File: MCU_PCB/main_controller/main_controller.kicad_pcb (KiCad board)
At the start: 2 copper layers, 127 x 101.7 mm, 62 parts, among them IC5 esp-12f, J1 TB006-508-05BE, J2 TB006-508-05BE, J4 TB006-508-05BE, J5 1715250000, J8 USB_B_Micro, Q2 S8050, Q3 S8050, SW1 SW_SPDT, U1 STM32F446ZET6, U3 CH340G, U4 R-78E5.0-0.5, U5 ISE0512A-H, X1 ECS-2520MV-xxx-xx, Y1 Crystal_GND24_Small

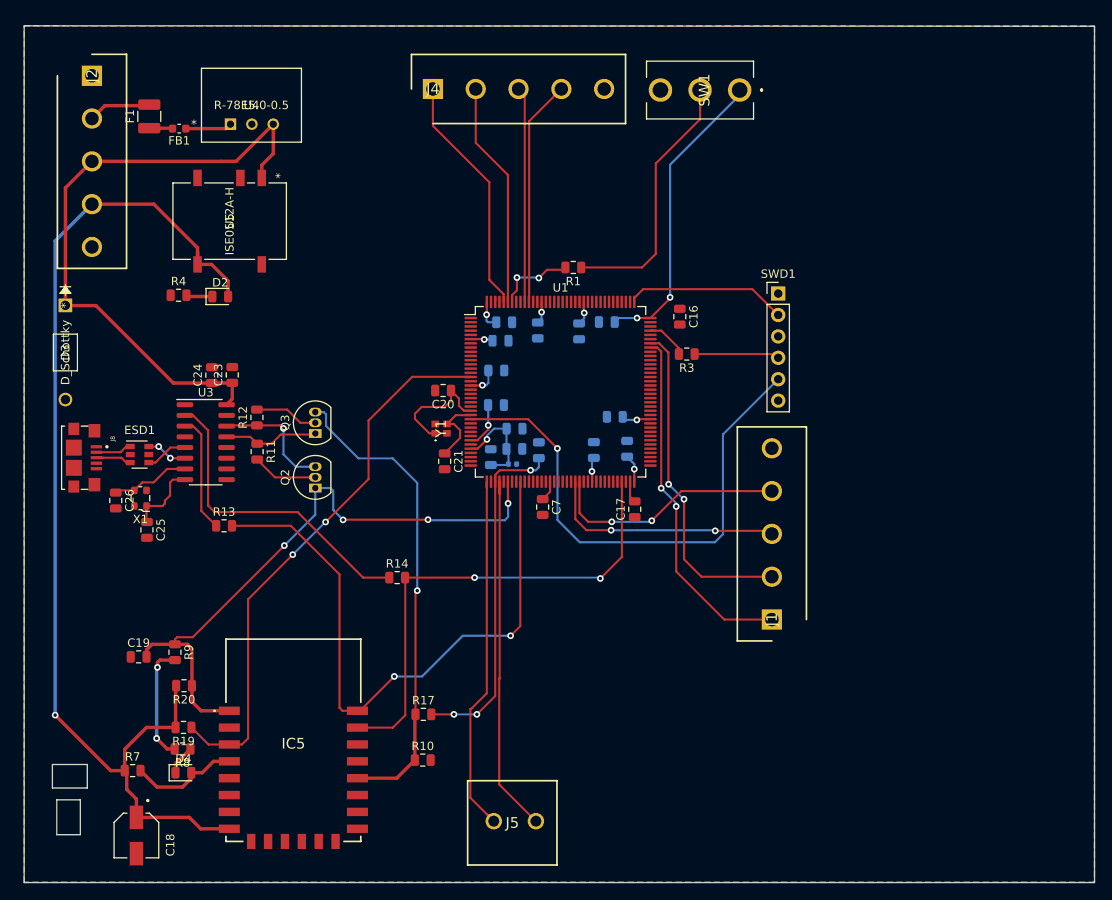
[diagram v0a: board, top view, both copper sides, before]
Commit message: finished drc check
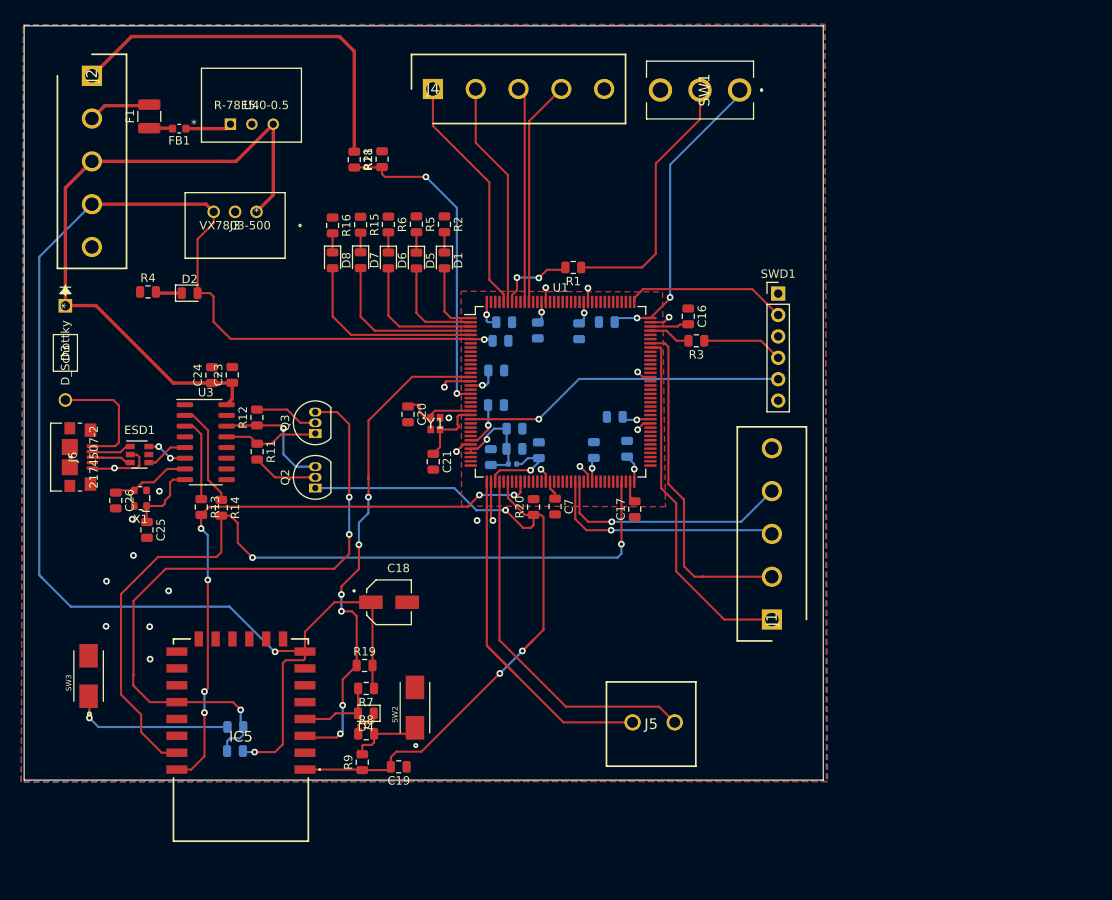
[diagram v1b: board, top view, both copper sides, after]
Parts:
- removed J8: USB_B_Micro, usbtomicro:J_SMD_2174507-2-5_7.8_5_2.71
- removed U5: ISE0512A-H, 5to3.3:ISE0512A-H
- added D1: LED, LED_SMD:LED_0805_2012Metric, F.Cu at (151.8, 54.7)
- added D5: LED, LED_SMD:LED_0805_2012Metric, F.Cu at (148.5, 54.7)
- added D6: LED, LED_SMD:LED_0805_2012Metric, F.Cu at (145.2, 54.7)
- added D7: LED, LED_SMD:LED_0805_2012Metric, F.Cu at (141.9, 54.7)
- added D8: LED, LED_SMD:LED_0805_2012Metric, F.Cu at (138.6, 54.7)
- added J3: VX7803-500, NEW5TO3V3:VX7803-500, F.Cu at (129.6, 49.0)
- added J6: 2174507-2, microusb_b:2174507-2, F.Cu at (107.7, 78.1)
- added R15: R, Resistor_SMD:R_0805_2012Metric, F.Cu at (141.9, 50.5)
- added R16: R, Resistor_SMD:R_0805_2012Metric, F.Cu at (138.6, 50.6)
- added R18: 10k, Resistor_SMD:R_0805_2012Metric, F.Cu at (141.2, 42.8)
- added R2: R, Resistor_SMD:R_0805_2012Metric, F.Cu at (151.8, 50.4)
- added R21: 2k, Resistor_SMD:R_0805_2012Metric, F.Cu at (144.4, 42.7)
- added R5: R, Resistor_SMD:R_0805_2012Metric, F.Cu at (148.5, 50.4)
- added R6: R, Resistor_SMD:R_0805_2012Metric, F.Cu at (145.2, 50.5)
- added SW2: KEY_USER, pushbutton:SW_147873-2, F.Cu at (148.3, 107.8)
- added SW3: KEY_FLASH, pushbutton:SW_147873-2, F.Cu at (109.6, 104.0)
- R10, R17: moved to B.Cu
- moved R20 46.6 mm to (162.4, 84.0), turned to 90 degrees
- moved C18 40.8 mm to (145.3, 95.3), turned to 0 degrees
- moved C19 33.5 mm to (146.4, 114.8), turned to 180 degrees
- moved R7 29.4 mm to (142.6, 105.5), turned to 180 degrees
- moved R9 25.8 mm to (142.1, 114.2), turned to 90 degrees
- moved R17 22.8 mm to (127.0, 112.9)
- moved D4 22.8 mm to (142.5, 108.5), turned to 180 degrees
- moved R19 22.7 mm to (142.4, 102.8), turned to 0 degrees
- moved R10 22.6 mm to (127.0, 110.1), turned to 180 degrees
- moved R14 22.4 mm to (125.4, 84.1), turned to 270 degrees
- moved R8 21.9 mm to (142.6, 110.9), turned to 0 degrees
- moved J5 20.2 mm to (179.2, 109.5)
- moved IC5 6.23 mm to (127.7, 111.6), turned to 180 degrees
- moved C20 5.03 mm to (147.5, 73.0), turned to 270 degrees
- moved D2 3.65 mm to (121.6, 58.6)
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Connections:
- U1 pad 1: Net-(U1-Pad1) -> GPIO_LED1
- U1 pad 2: Net-(U1-Pad2) -> GPIO_LED2
- U1 pad 3: Net-(U1-Pad3) -> GPIO_LED3
- U1 pad 35: TIM2_CH2 -> Net-(U1-Pad35)
- U1 pad 4: Net-(U1-Pad4) -> GPIO_LED4
- U1 pad 5: Net-(U1-Pad5) -> GPIO_LED5
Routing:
- net 12V: track 0.00 -> 45.7 mm
- net USART1_TX: track 58.4 -> 100.6 mm
- net ADC3_IN5: track 0.00 -> 38.4 mm, vias 0 -> 2
- net GND: track 0.00 -> 32.0 mm, vias 0 -> 21
- net Net-(R14-Pad1): track 37.9 -> 12.8 mm
- net 3V3: track 240.6 -> 264.8 mm, vias 15 -> 14
- net NRST: track 62.5 -> 38.5 mm
- net GPIO_LED5: track 0.00 -> 23.0 mm
- net /WiFi + MCU/GPIO0: track 57.3 -> 78.6 mm, vias 1 -> 3
- net Net-(R10-Pad2): track 0.00 -> 20.1 mm, vias 0 -> 1
- net GPIO_LED4: track 0.00 -> 19.5 mm
- net GPIO_LED3: track 0.00 -> 15.9 mm
- net Net-(D3-Pad2): track 0.00 -> 15.3 mm
- net WIFI_nRST: track 75.0 -> 87.5 mm, vias 4 -> 3
- net GPIO_LED2: track 0.00 -> 12.2 mm
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- added copper zone on F.Cu, net 3V3
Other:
- board size 127 x 101.7 mm -> 94.8 x 89.5 mm

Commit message: Adding footprints/schematics locally
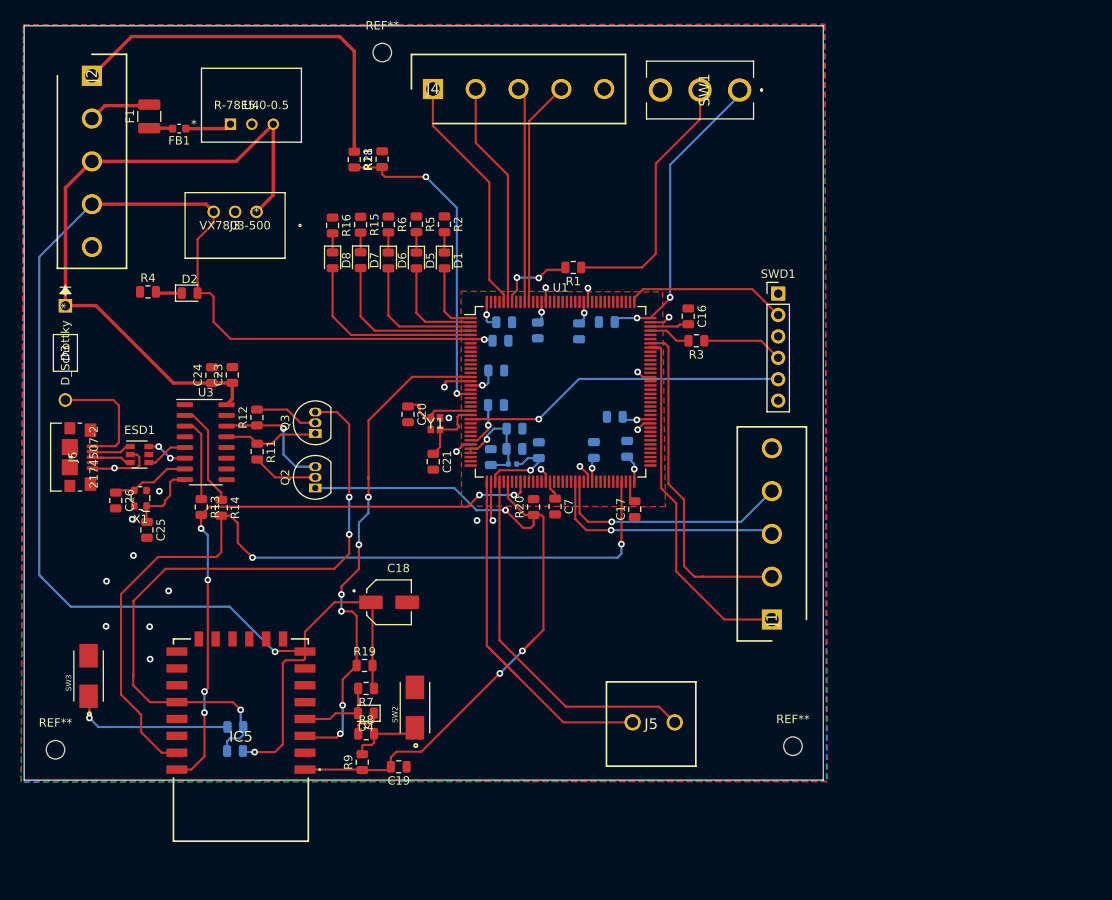
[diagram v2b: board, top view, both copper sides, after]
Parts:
- added REF**: MountingHole_2.2mm_M2, MountingHole:MountingHole_2.2mm_M2, F.Cu at (144.5, 30.1)
- added REF**: MountingHole_2.2mm_M2, MountingHole:MountingHole_2.2mm_M2, F.Cu at (105.7, 112.8)
- added REF**: MountingHole_2.2mm_M2, MountingHole:MountingHole_2.2mm_M2, F.Cu at (193.2, 112.3)
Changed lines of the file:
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@@
   (general
     (thickness 1.6)
-    (drawings 4)
+    (drawings 8)
     (tracks 606)
     (zones 0)
-    (modules 76)
+    (modules 79)
     (nets 185)
   )
@@
     (add_net WIFI_nRST)
   )
+  (module MountingHole:MountingHole_2.2mm_M2 (layer F.Cu)
+    (at 144.475 30.05)
+    (descr "Mounting Hole 2.2mm, no annular, M2")
+    (tags "mounting hole 2.2mm no annular m2")
+    (attr virtual)
+    (fp_text reference REF** (at 0 -3.2) (layer F.SilkS)
+      (effects (font (size 1 1) (thickness 0.15)))
+    )
+    (fp_text value MountingHole_2.2mm_M2 (at 0 3.2) (layer F.Fab)
+      (effects (font (size 1 1) (thickness 0.15)))
+    )
+    (fp_circle (center 0 0) (end 2.2 0) (layer Cmts.User) (width 0.15))
+    (fp_circle (center 0 0) (end 2.45 0) (layer F.CrtYd) (width 0.05))
+    (fp_text user %R (at 0.3 0) (layer F.Fab)
+      (effects (font (size 1 1) (thickness 0.15)))
+    )
+    (pad 1 np_thru_hole circle (at 0 0) (size 2.2 2.2) (drill 2.2) (layers *.Cu *.Mask))
+  )
+  (module MountingHole:MountingHole_2.2mm_M2 (layer F.Cu)
+    (at 105.7 112.775)
+    (descr "Mounting Hole 2.2mm, no annular, M2")
+    (tags "mounting hole 2.2mm no annular m2")
+    (attr virtual)
+    (fp_text reference REF** (at 0 -3.2) (layer F.SilkS)
+      (effects (font (size 1 1) (thickness 0.15)))
+    )
+    (fp_text value MountingHole_2.2mm_M2 (at 0 3.2) (layer F.Fab)
+      (effects (font (size 1 1) (thickness 0.15)))
+    )
+    (fp_circle (center 0 0) (end 2.2 0) (layer Cmts.User) (width 0.15))
+    (fp_circle (center 0 0) (end 2.45 0) (layer F.CrtYd) (width 0.05))
+    (fp_text user %R (at 0.3 0) (layer F.Fab)
+      (effects (font (size 1 1) (thickness 0.15)))
+    )
+    (pad 1 np_thru_hole circle (at 0 0) (size 2.2 2.2) (drill 2.2) (layers *.Cu *.Mask))
+  )
+  (module MountingHole:MountingHole_2.2mm_M2 (layer F.Cu)
+    (at 193.2 112.35)
+    (descr "Mounting Hole 2.2mm, no annular, M2")
+    (tags "mounting hole 2.2mm no annular m2")
+    (attr virtual)
+    (fp_text reference REF** (at 0 -3.2) (layer F.SilkS)
+      (effects (font (size 1 1) (thickness 0.15)))
+    )
+    (fp_text value MountingHole_2.2mm_M2 (at 0 3.2) (layer F.Fab)
+      (effects (font (size 1 1) (thickness 0.15)))
+    )
+    (fp_circle (center 0 0) (end 2.2 0) (layer Cmts.User) (width 0.15))
+    (fp_circle (center 0 0) (end 2.45 0) (layer F.CrtYd) (width 0.05))
+    (fp_text user %R (at 0.3 0) (layer F.Fab)
+      (effects (font (size 1 1) (thickness 0.15)))
+    )
+    (pad 1 np_thru_hole circle (at 0 0) (size 2.2 2.2) (drill 2.2) (layers *.Cu *.Mask))
+  )
   (module NEW5TO3V3:VX7803-500 (layer F.Cu)
     (at 129.55 48.95 180)
@@
       (net 184 "Net-(J6-Pad11)"))
   )
+  (gr_circle (center 138.45 115.075) (end 138.5 115.6) (layer Dwgs.User) (width 0.15))
+  (gr_circle (center 113.05 76.8) (end 113.1 77.325) (layer Dwgs.User) (width 0.15))
+  (gr_circle (center 118.9 71.85) (end 118.95 72.375) (layer Dwgs.User) (width 0.15))
+  (gr_circle (center 153.125 61.45) (end 153.175 61.975) (layer Dwgs.User) (width 0.15))
   (gr_line (start 196.8 26.88) (end 101.983 26.88) (layer Edge.Cuts) (width 0.05))
   (gr_line (start 196.8 116.375) (end 196.8 26.88) (layer Edge.Cuts) (width 0.05))

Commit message: Archived main board
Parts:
- removed the REF** at (144.5, 30.1)
- removed the REF** at (105.7, 112.8)
- removed the REF** at (193.2, 112.3)
- added R22: 0, Resistor_SMD:R_0805_2012Metric, B.Cu at (161.4, 71.4)
- added REF**: MountingHole_2.2mm_M2, MountingHole:MountingHole_2.2mm_M2, F.Cu at (143.0, 32.7)
- added REF**: MountingHole_2.2mm_M2, MountingHole:MountingHole_2.2mm_M2, F.Cu at (192.0, 111.8)
- added REF**: MountingHole_2.2mm_M2, MountingHole:MountingHole_2.2mm_M2, F.Cu at (105.9, 113.2)
- D3: footprint Diode 4007:1N4007G-T -> walle_library:1N4007G-T
- IC5: footprint esp12f -> walle_library:esp12f
- J3: footprint NEW5TO3V3:VX7803-500 -> walle_library:VX7803-500
- J6: footprint microusb_b:2174507-2 -> walle_library:2174507-2
- SW1: footprint spdt switch:118251376 -> walle_library:118251376
- SW2, SW3: footprint pushbutton:SW_147873-2 -> walle_library:SW_147873-2
- U4: footprint DC 7.5 to 5:R-78E5.0-0.5 -> walle_library:R-78E5.0-0.5
- Y1: footprint EA1620LA12-16.000M_TR:EA1620LA1216000MTR -> walle_library:EA1620LA1216000MTR
- moved R18 3.75 mm to (138.6, 45.5)
- moved R21 3.75 mm to (141.9, 45.4)
- moved C15 2.45 mm to (160.2, 74.6), turned to 180 degrees
- moved C14 2.35 mm to (160.2, 77.0), turned to 180 degrees
- moved C5 1.40 mm to (157.4, 76.7)
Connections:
- C14 pad 2: GND -> /AGND
- C15 pad 2: GND -> /AGND
- C5 pad 2: GND -> /AGND
- SWD1 pad 1: 3.3V_regulator -> 3V3
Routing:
- net 3V3: track 264.8 -> 282.2 mm, vias 14 -> 16
- net /AGND: track 0.00 -> 9.73 mm
- net +3.3VA: track 12.4 -> 14.0 mm
- net ADC3_IN5: track 38.4 -> 39.0 mm
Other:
- board text added: "+"

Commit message: Increasing 5V Trace
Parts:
- removed REF** (x3): MountingHole_2.2mm_M2, MountingHole:MountingHole_2.2mm_M2
- added H1: MountingHole, MountingHole:MountingHole_2.2mm_M2, F.Cu at (105.8, 113.1)
- added H2: MountingHole, MountingHole:MountingHole_2.2mm_M2, F.Cu at (191.6, 111.3)
- added H3: MountingHole, MountingHole:MountingHole_2.2mm_M2, F.Cu at (142.8, 34.2)
- added TP1: TestPoint, TestPoint:TestPoint_Loop_D2.50mm_Drill1.0mm, F.Cu at (104.6, 103.1)
- added TP2: TestPoint, TestPoint:TestPoint_Loop_D2.50mm_Drill1.0mm, F.Cu at (104.6, 107.7)
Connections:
- net /WiFi + MCU/ADC renamed Net-(IC5-Pad2)
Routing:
- net USART1_TX: track 100.6 -> 124.6 mm
- net 5V: track 79.5 -> 56.2 mm
- net USART1_RX: track 73.5 -> 92.0 mm
- added copper zone on F.Cu, net 5V

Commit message: Final
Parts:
- removed U4: R-78E5.0-0.5, walle_library:R-78E5.0-0.5
- added C22: 10uF, Capacitor_SMD:C_1210_3225Metric, F.Cu at (134.6, 43.0)
- added C27: 22uF, Capacitor_SMD:C_1210_3225Metric, F.Cu at (118.3, 51.2)
- added C28: 10uF, Capacitor_SMD:C_1210_3225Metric, F.Cu at (128.2, 43.0)
- added C29: 10uF, Capacitor_SMD:C_1210_3225Metric, B.Cu at (131.9, 33.9)
- added PS1: R-78E5.0-1.0, R78E5010, F.Cu at (126.7, 37.6)
- moved FB1 3.67 mm to (118.5, 42.2)
- moved R12 0.10 mm to (129.5, 73.4)
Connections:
- ESD1 pad 5: +5V -> (no net)
- IC5 pad 10: Net-(IC5-Pad10) -> (no net)
- IC5 pad 11: Net-(IC5-Pad11) -> (no net)
- IC5 pad 12: Net-(IC5-Pad12) -> (no net)
- IC5 pad 13: Net-(IC5-Pad13) -> (no net)
- IC5 pad 14: Net-(IC5-Pad14) -> (no net)
- IC5 pad 16: Net-(IC5-Pad16) -> (no net)
- IC5 pad 17: Net-(IC5-Pad17) -> (no net)
- IC5 pad 19: Net-(IC5-Pad19) -> (no net)
- IC5 pad 2: Net-(IC5-Pad2) -> (no net)
- IC5 pad 20: Net-(IC5-Pad20) -> (no net)
- IC5 pad 5: Net-(IC5-Pad5) -> (no net)
- IC5 pad 6: Net-(IC5-Pad6) -> (no net)
- IC5 pad 7: Net-(IC5-Pad7) -> (no net)
- IC5 pad 9: Net-(IC5-Pad9) -> (no net)
- J6 pad 10: Net-(J6-Pad10) -> (no net)
- J6 pad 11: Net-(J6-Pad11) -> (no net)
- J6 pad 4: Net-(J6-Pad4) -> (no net)
- J6 pad 6: Net-(J6-Pad6) -> (no net)
- J6 pad 7: Net-(J6-Pad7) -> (no net)
- J6 pad 8: Net-(J6-Pad8) -> (no net)
- J6 pad 9: Net-(J6-Pad9) -> (no net)
- Q2 pad 1: WIFI_nRST -> Net-(Q2-Pad1)
- Q2 pad 3: Net-(Q2-Pad3) -> WIFI_nRST
- R12 pad 1: Net-(Q2-Pad3) -> Net-(Q2-Pad1)
- SWD1 pad 6: Net-(SWD1-Pad6) -> (no net)
- U1 pad 10: Net-(U1-Pad10) -> (no net)
- U1 pad 100: Net-(U1-Pad100) -> (no net)
- U1 pad 103: Net-(U1-Pad103) -> (no net)
- U1 pad 104: Net-(U1-Pad104) -> (no net)
- U1 pad 11: Net-(U1-Pad11) -> (no net)
- U1 pad 110: Net-(U1-Pad110) -> (no net)
- U1 pad 111: Net-(U1-Pad111) -> (no net)
- U1 pad 112: Net-(U1-Pad112) -> (no net)
- U1 pad 113: Net-(U1-Pad113) -> (no net)
- U1 pad 114: Net-(U1-Pad114) -> (no net)
- U1 pad 115: Net-(U1-Pad115) -> (no net)
- U1 pad 116: Net-(U1-Pad116) -> (no net)
- U1 pad 117: Net-(U1-Pad117) -> (no net)
- U1 pad 118: Net-(U1-Pad118) -> (no net)
- U1 pad 119: Net-(U1-Pad119) -> (no net)
- U1 pad 12: Net-(U1-Pad12) -> (no net)
- U1 pad 122: Net-(U1-Pad122) -> (no net)
- U1 pad 123: Net-(U1-Pad123) -> (no net)
- U1 pad 124: Net-(U1-Pad124) -> (no net)
- U1 pad 125: Net-(U1-Pad125) -> (no net)
- U1 pad 126: Net-(U1-Pad126) -> (no net)
- U1 pad 127: Net-(U1-Pad127) -> (no net)
- U1 pad 128: Net-(U1-Pad128) -> (no net)
- U1 pad 129: Net-(U1-Pad129) -> (no net)
- U1 pad 13: Net-(U1-Pad13) -> (no net)
- U1 pad 132: Net-(U1-Pad132) -> (no net)
- U1 pad 133: Net-(U1-Pad133) -> (no net)
- U1 pad 136: Net-(U1-Pad136) -> (no net)
- U1 pad 137: Net-(U1-Pad137) -> (no net)
- U1 pad 14: Net-(U1-Pad14) -> (no net)
- U1 pad 141: Net-(U1-Pad141) -> (no net)
- U1 pad 142: Net-(U1-Pad142) -> (no net)
- U1 pad 143: Net-(U1-Pad143) -> (no net)
- U1 pad 18: Net-(U1-Pad18) -> (no net)
- U1 pad 20: Net-(U1-Pad20) -> (no net)
- U1 pad 21: Net-(U1-Pad21) -> (no net)
- U1 pad 22: Net-(U1-Pad22) -> (no net)
- U1 pad 26: Net-(U1-Pad26) -> (no net)
- U1 pad 27: Net-(U1-Pad27) -> (no net)
- U1 pad 28: Net-(U1-Pad28) -> (no net)
- U1 pad 29: Net-(U1-Pad29) -> (no net)
- U1 pad 34: Net-(U1-Pad34) -> (no net)
- U1 pad 35: Net-(U1-Pad35) -> (no net)
- U1 pad 36: ADC123_IN2 -> (no net)
- U1 pad 41: DAC_OUT2 -> (no net)
- U1 pad 43: Net-(U1-Pad43) -> (no net)
- U1 pad 44: Net-(U1-Pad44) -> (no net)
- U1 pad 46: Net-(U1-Pad46) -> (no net)
- U1 pad 47: Net-(U1-Pad47) -> (no net)
- U1 pad 48: TIM2_CH4 -> (no net)
- U1 pad 49: Net-(U1-Pad49) -> (no net)
- U1 pad 50: Net-(U1-Pad50) -> (no net)
- U1 pad 53: Net-(U1-Pad53) -> (no net)
- U1 pad 54: Net-(U1-Pad54) -> (no net)
- U1 pad 55: Net-(U1-Pad55) -> (no net)
- U1 pad 56: Net-(U1-Pad56) -> (no net)
- U1 pad 57: Net-(U1-Pad57) -> (no net)
- U1 pad 60: Net-(U1-Pad60) -> (no net)
- U1 pad 63: Net-(U1-Pad63) -> (no net)
- U1 pad 64: Net-(U1-Pad64) -> (no net)
- U1 pad 65: Net-(U1-Pad65) -> (no net)
- U1 pad 66: Net-(U1-Pad66) -> (no net)
- U1 pad 67: Net-(U1-Pad67) -> (no net)
- U1 pad 68: Net-(U1-Pad68) -> (no net)
- U1 pad 7: Net-(U1-Pad7) -> (no net)
- U1 pad 70: Net-(U1-Pad70) -> (no net)
- U1 pad 73: Net-(U1-Pad73) -> (no net)
- U1 pad 74: Net-(U1-Pad74) -> (no net)
- U1 pad 75: Net-(U1-Pad75) -> (no net)
- U1 pad 76: Net-(U1-Pad76) -> (no net)
- U1 pad 77: Net-(U1-Pad77) -> (no net)
- U1 pad 78: Net-(U1-Pad78) -> (no net)
- U1 pad 79: Net-(U1-Pad79) -> (no net)
- U1 pad 8: Net-(U1-Pad8) -> (no net)
- U1 pad 80: Net-(U1-Pad80) -> (no net)
- U1 pad 81: Net-(U1-Pad81) -> (no net)
- U1 pad 82: Net-(U1-Pad82) -> (no net)
- U1 pad 85: TIM4_CH3 -> (no net)
- U1 pad 86: TIM4_CH4 -> (no net)
- U1 pad 87: Net-(U1-Pad87) -> (no net)
- U1 pad 88: Net-(U1-Pad88) -> (no net)
- U1 pad 89: Net-(U1-Pad89) -> (no net)
- U1 pad 9: Net-(U1-Pad9) -> (no net)
- U1 pad 90: Net-(U1-Pad90) -> (no net)
- U1 pad 91: Net-(U1-Pad91) -> (no net)
- U1 pad 92: Net-(U1-Pad92) -> (no net)
- U1 pad 93: Net-(U1-Pad93) -> (no net)
- U1 pad 95: Net-(U1-Pad95) -> (no net)
- U1 pad 96: Net-(U1-Pad96) -> (no net)
- U1 pad 97: Net-(U1-Pad97) -> (no net)
- U1 pad 98: TIM3_CH3 -> (no net)
- U1 pad 99: TIM3_CH4 -> (no net)
- U3 pad 10: Net-(U3-Pad10) -> (no net)
- U3 pad 11: Net-(U3-Pad11) -> (no net)
- U3 pad 12: Net-(U3-Pad12) -> (no net)
- U3 pad 14: Net-(Q2-Pad3) -> Net-(Q2-Pad1)
- U3 pad 15: Net-(U3-Pad15) -> (no net)
- U3 pad 4: Net-(U3-Pad4) -> (no net)
- U3 pad 9: Net-(U3-Pad9) -> (no net)
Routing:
- net 5V: track 56.2 -> 83.6 mm
- net Net-(Q2-Pad1): track 0.00 -> 17.7 mm, vias 0 -> 1
- net Net-(Q2-Pad3): track 14.4 -> 0.00 mm, vias 1 -> 0
- net 7.5V: track 5.51 -> 14.8 mm
- net 3V3: track 282.2 -> 289.9 mm
- net GND: track 32.0 -> 37.5 mm
- net WIFI_nRST: track 87.5 -> 89.4 mm
- net Net-(F1-Pad1): track 2.78 -> 4.02 mm
